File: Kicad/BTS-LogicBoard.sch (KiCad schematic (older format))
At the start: 54 parts, among them J1 Conn_01x06, J2 Conn_01x04, J3 Conn_01x02, Q1 BC817, Q3 BC817, Q4 BC807, Q5 BC817, Q6 BC817, SW1 SW_DPDT_x2, SW2 SW_DPDT_x2, U1 NCS2252SN2T1G, U2 NE555D, U3 NCS2252SN2T1G, U4 TLP291

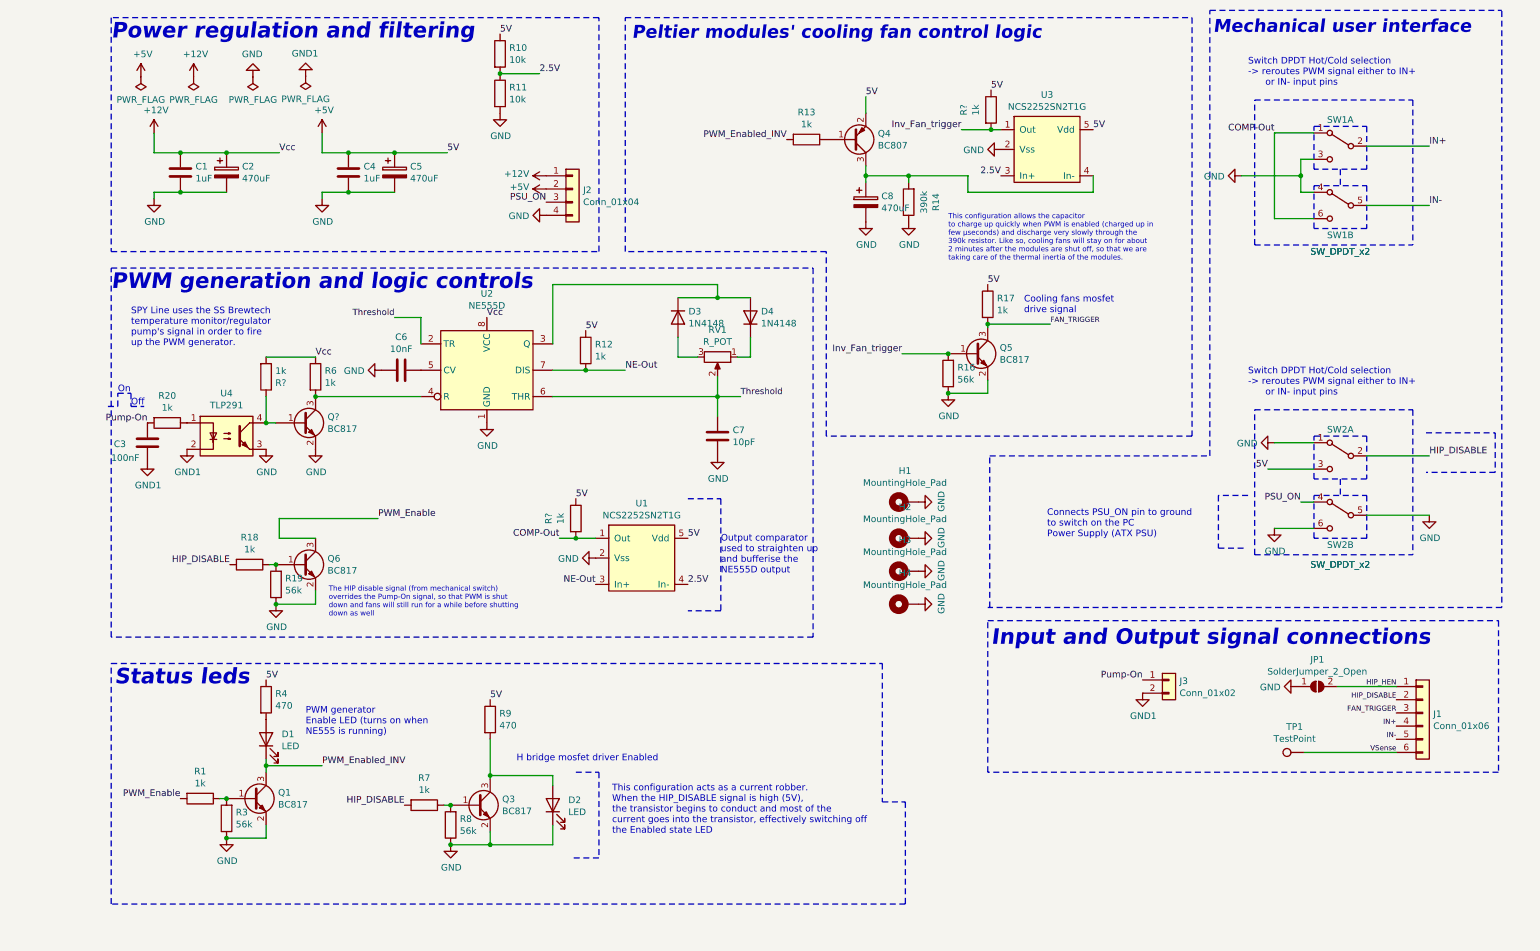
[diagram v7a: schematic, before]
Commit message: Updated schematic with proper inverter (not gates) logic layout
Signed-off-by: bebenlebricolo <benoittarrade@hotmail.fr>
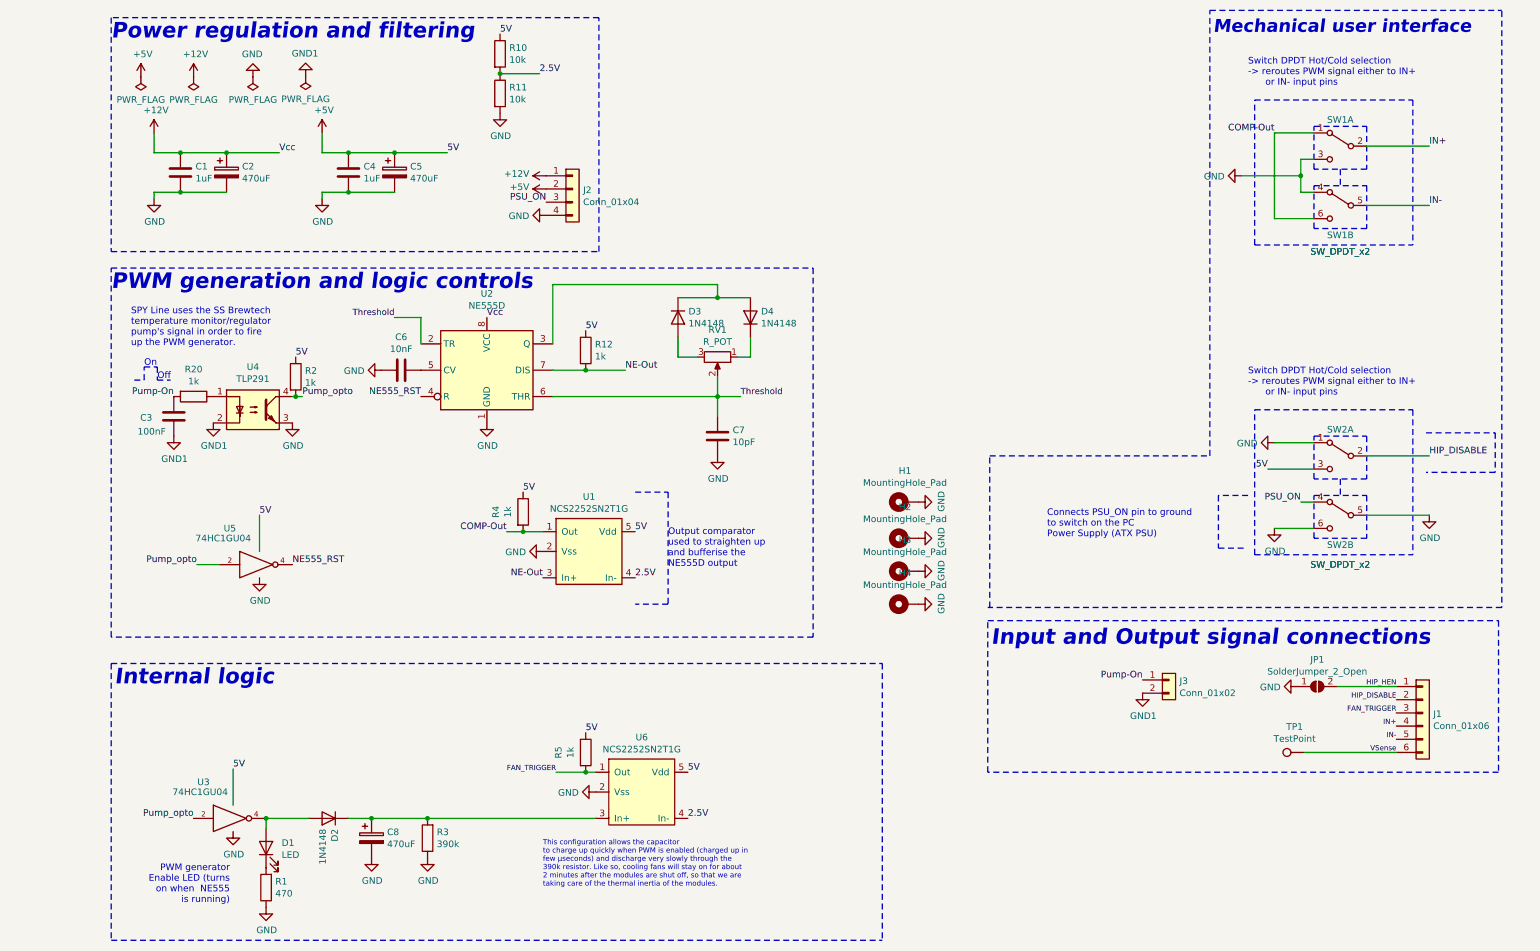
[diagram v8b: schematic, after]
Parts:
- removed D2: LED, LED_THT:LED_D3.0mm, symbol Device:LED
- removed Q1, Q3, Q5, Q6, Q?: BC817, Package_TO_SOT_SMD:SOT-23, symbol Transistor_BJT:BC817
- removed Q4: BC807, Package_TO_SOT_SMD:SOT-23, symbol Transistor_BJT:BC807
- removed R13, R17, R18, R6, R7, R? (x2): 1k, Resistor_SMD:R_1206_3216Metric_Pad1.30x1.75mm_HandSolder, symbol Device:R
- removed R14: 390k, Resistor_SMD:R_1206_3216Metric_Pad1.30x1.75mm_HandSolder, symbol Device:R
- removed R16, R19, R8: 56k, Resistor_SMD:R_1206_3216Metric_Pad1.30x1.75mm_HandSolder, symbol Device:R
- removed R4, R9: 470, Resistor_SMD:R_1206_3216Metric_Pad1.30x1.75mm_HandSolder, symbol Device:R
- removed U3: NCS2252SN2T1G, Package_TO_SOT_SMD:SOT-23-5, symbol BTS-LogicBoard:NCS2252SN2T1G
- added D2: 1N4148, Diode_SMD:D_1206_3216Metric_Pad1.42x1.75mm_HandSolder, symbol Diode:1N4148
- added R2, R5: 1k, Resistor_SMD:R_1206_3216Metric_Pad1.30x1.75mm_HandSolder, symbol Device:R
- added U3: 74HC1GU04, Package_TO_SOT_SMD:SOT-353_SC-70-5_Handsoldering, symbol 74xGxx:74AHC1GU04
- added U5: 74HC1GU04, Package_TO_SOT_SMD:SOT-353_SC-70-5, symbol 74xGxx:74AHC1GU04
- added U6: NCS2252SN2T1G, Package_TO_SOT_SMD:SOT-23-5, symbol BTS-LogicBoard:NCS2252SN2T1G
- R1: value 1k -> 470
- R3: value 56k -> 390k
- gave numbers to parts that had none: 1
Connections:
- net PWM_Enabled_INV is gone; now on an unnamed net: D1.1 (K)
- net +5V: now also R2.1, R5.1, U3.5 (VCC), U5.5 (VCC), U6.5 (Vdd)
- net 2.5V: now also U6.4 (In-)
- net FAN_TRIGGER: now also R5.2, U6.1 (Out)
- net GND: now also R1.1, U3.3 (GND), U5.3 (GND), U6.2 (Vss)
- net NE555_RST: now reaches U2.4 (R)
- net NE555_RST: now also U5.4
- net at R3.2: now also C8.1, D2.1 (K), U6.3 (In+); no longer R1.1
- net at D1.2 (A): now also D2.2 (A), U3.4
- net Pump_opto: now reaches U4.4
- net Pump_opto: now also R2.2, U3.2, U5.2
- net PWM_Enable: no longer names the net of R1.2
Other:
- note added: "Internal logic"
- note added: "PWM generator \nEnable LED (turns \non when NE555 \nis running)"
- note removed: "Cooling fans mosfet \ndrive signal"
- note removed: "H bridge mosfet driver Enabled"
- note removed: "PWM generator \nEnable LED (turns on when \nNE555 is running)"
- note removed: "Peltier modules' cooling fan control logic"
- note removed: "Status leds"
- note removed: "The HIP disable signal (from mechanical switch)\noverrides the Pump-On signal, so that PWM is shut\ndown and fans will still run for a while before shutting\ndown as well"
- note removed: "This configuration acts as a current robber.\nWhen the HIP_DISABLE signal is high (5V),\nthe transistor begins to conduct and most of the\ncurrent goes into the transistor, effectively switching off\nthe Enabled state LED"
- moved on the sheet: C3, D1, R20, R4, U1, U4
